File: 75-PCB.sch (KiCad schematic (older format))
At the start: 193 parts

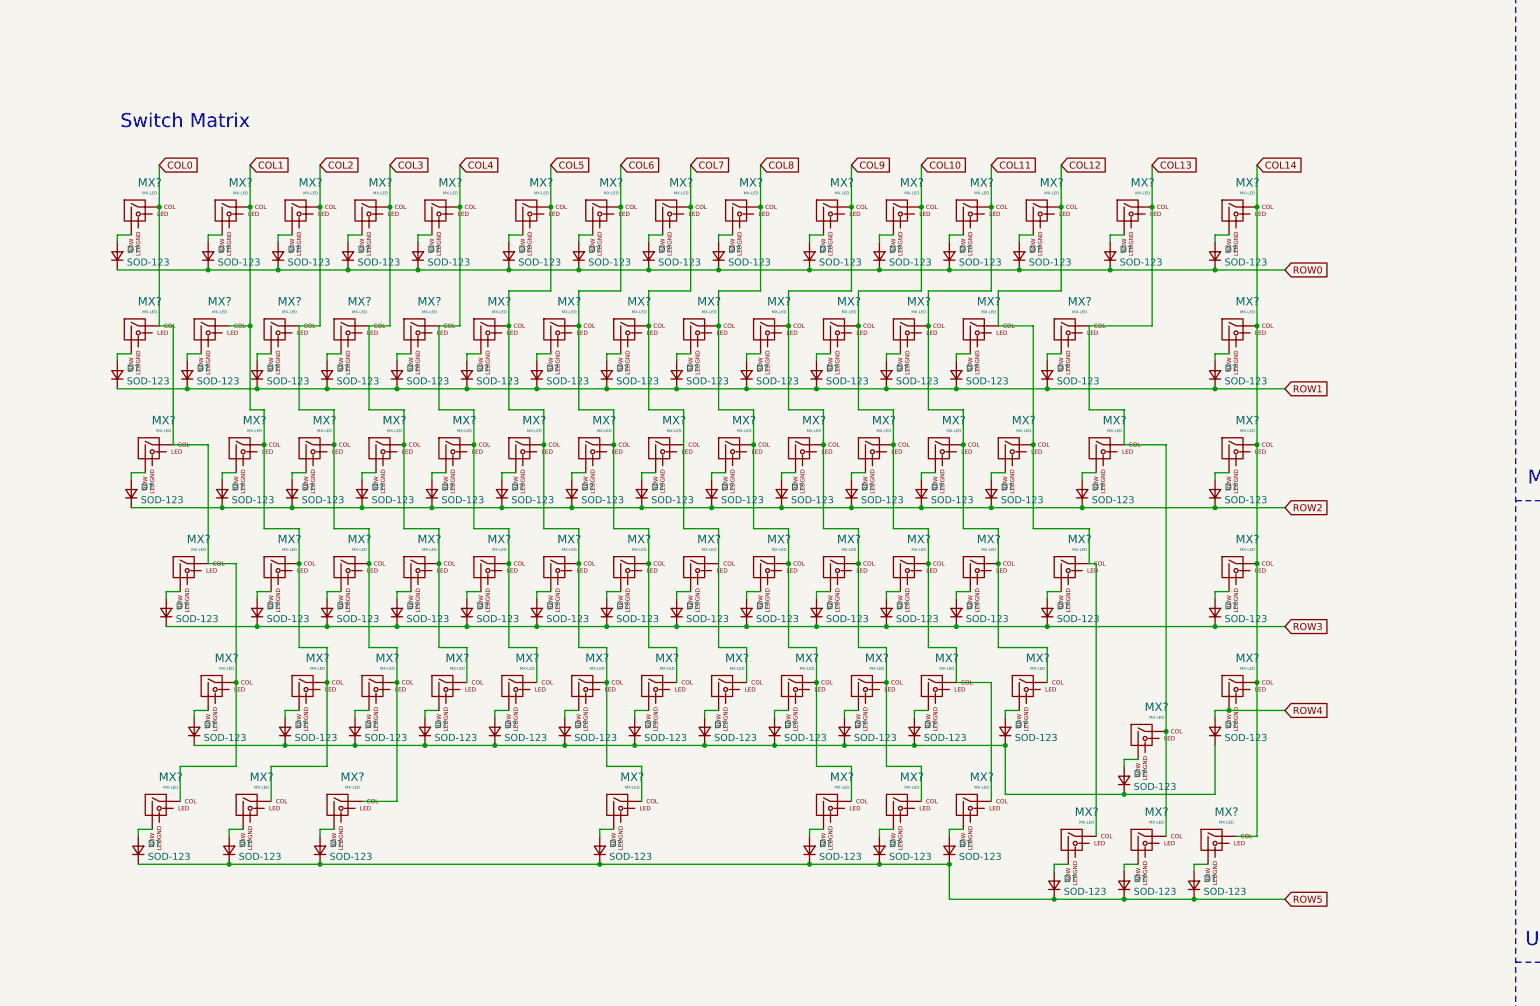
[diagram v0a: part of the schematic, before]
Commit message: Changed layout of switch matrix in schematic
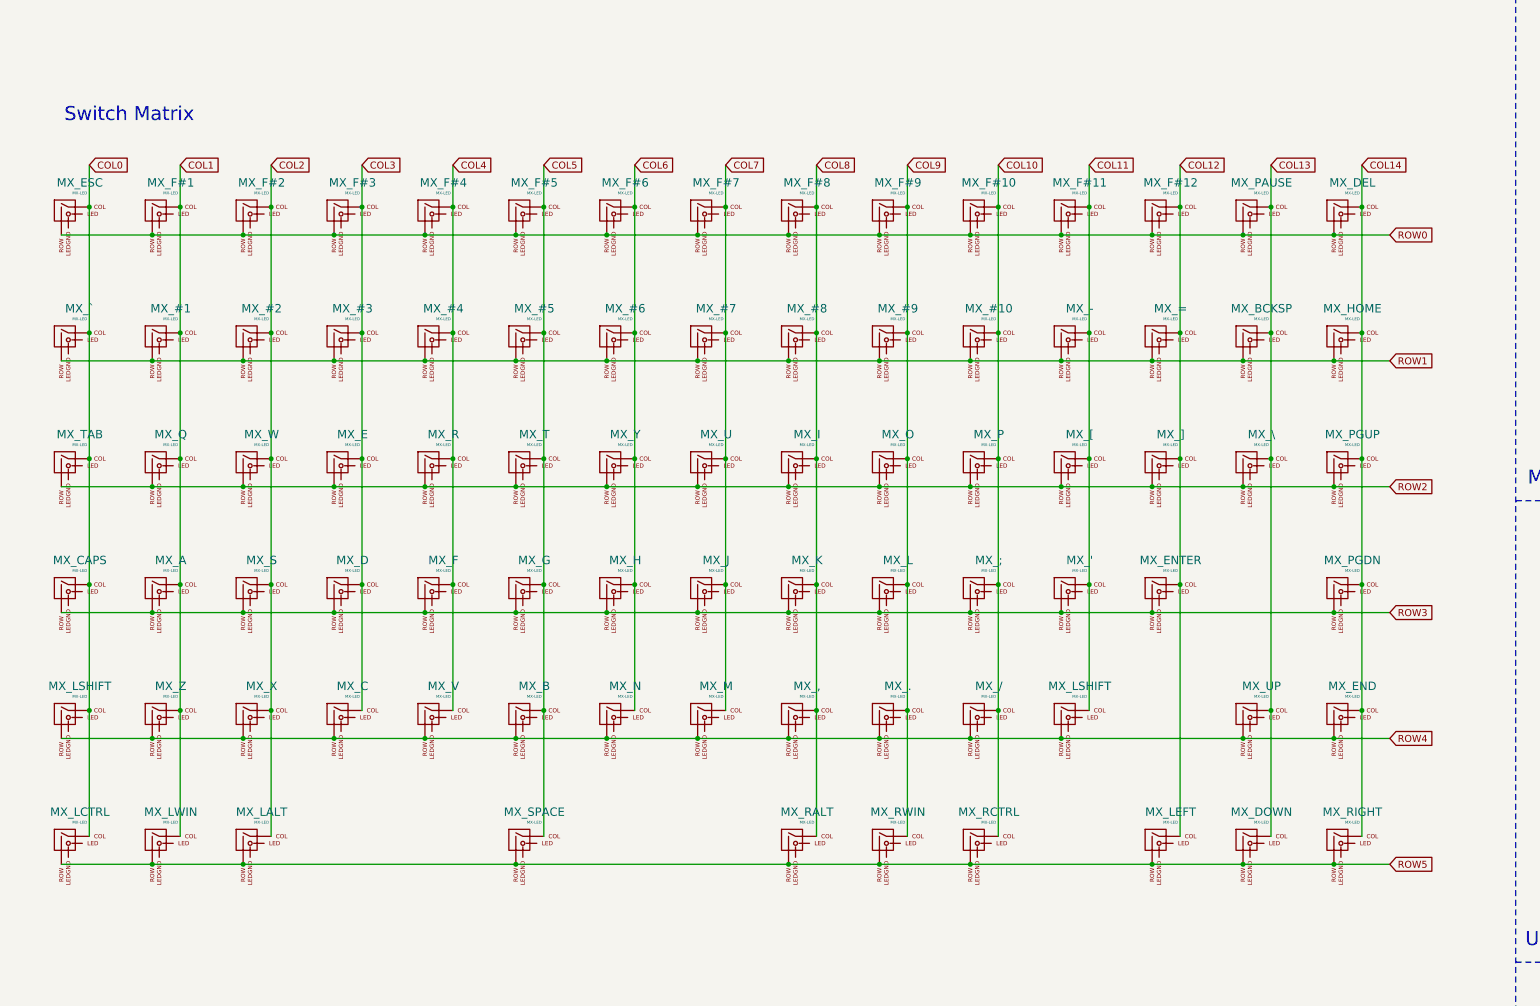
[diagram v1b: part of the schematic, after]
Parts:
- removed D? (x83): SOD-123, symbol Device:D_Small
- removed MX? (x83): MX-LED, symbol MX_Alps_Hybrid:MX-LED
- added MX_#1, MX_#10, MX_#2, MX_#3, MX_#4, MX_#5, MX_#6, MX_#7, MX_#8, MX_#9, MX_', MX_,, MX_-, MX_., MX_/, MX_;, MX_=, MX_A, MX_B, MX_BCKSP, MX_C, MX_CAPS, MX_D, MX_DEL, MX_DOWN, MX_E, MX_END, MX_ENTER, MX_ESC, MX_F, MX_F#1, MX_F#10, MX_F#11, MX_F#12, MX_F#2, MX_F#3, MX_F#4, MX_F#5, MX_F#6, MX_F#7, MX_F#8, MX_F#9, MX_G, MX_H, MX_HOME, MX_I, MX_J, MX_K, MX_L, MX_LALT, MX_LCTRL, MX_LEFT, MX_LSHIFT (x2), MX_LWIN, MX_M, MX_N, MX_O, MX_P, MX_PAUSE, MX_PGDN, MX_PGUP, MX_Q, MX_R, MX_RALT, MX_RCTRL, MX_RIGHT, MX_RWIN, MX_S, MX_SPACE, MX_T, MX_TAB, MX_U, MX_UP, MX_V, MX_W, MX_X, MX_Y, MX_Z, MX_[, MX_\, MX_], MX_`: MX-LED, symbol MX_Alps_Hybrid:MX-LED
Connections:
- net COL0: now also MX_CAPS.1 (COL), MX_ESC.1 (COL), MX_LCTRL.1 (COL), MX_LSHIFT.1 (COL), MX_TAB.1 (COL), MX_`.1 (COL)
- net COL1: now also MX_#1.1 (COL), MX_A.1 (COL), MX_F#1.1 (COL), MX_LWIN.1 (COL), MX_Q.1 (COL), MX_Z.1 (COL)
- net COL10: now also MX_#10.1 (COL), MX_/.1 (COL), MX_;.1 (COL), MX_F#10.1 (COL), MX_P.1 (COL), MX_RCTRL.1 (COL)
- net COL11: now also MX_'.1 (COL), MX_-.1 (COL), MX_F#11.1 (COL), MX_LSHIFT.1 (COL), MX_[.1 (COL)
- net COL12: now also MX_=.1 (COL), MX_ENTER.1 (COL), MX_F#12.1 (COL), MX_LEFT.1 (COL), MX_].1 (COL)
- net COL13: now also MX_BCKSP.1 (COL), MX_DOWN.1 (COL), MX_PAUSE.1 (COL), MX_UP.1 (COL), MX_\.1 (COL)
- net COL14: now also MX_DEL.1 (COL), MX_END.1 (COL), MX_HOME.1 (COL), MX_PGDN.1 (COL), MX_PGUP.1 (COL), MX_RIGHT.1 (COL)
- net COL2: now also MX_#2.1 (COL), MX_F#2.1 (COL), MX_LALT.1 (COL), MX_S.1 (COL), MX_W.1 (COL), MX_X.1 (COL)
- net COL3: now also MX_#3.1 (COL), MX_C.1 (COL), MX_D.1 (COL), MX_E.1 (COL), MX_F#3.1 (COL)
- net COL4: now also MX_#4.1 (COL), MX_F#4.1 (COL), MX_F.1 (COL), MX_R.1 (COL), MX_V.1 (COL)
- net COL5: now also MX_#5.1 (COL), MX_B.1 (COL), MX_F#5.1 (COL), MX_G.1 (COL), MX_SPACE.1 (COL), MX_T.1 (COL)
- net COL6: now also MX_#6.1 (COL), MX_F#6.1 (COL), MX_H.1 (COL), MX_N.1 (COL), MX_Y.1 (COL)
- net COL7: now also MX_#7.1 (COL), MX_F#7.1 (COL), MX_J.1 (COL), MX_M.1 (COL), MX_U.1 (COL)
- net COL8: now also MX_#8.1 (COL), MX_,.1 (COL), MX_F#8.1 (COL), MX_I.1 (COL), MX_K.1 (COL), MX_RALT.1 (COL)
- net COL9: now also MX_#9.1 (COL), MX_..1 (COL), MX_F#9.1 (COL), MX_L.1 (COL), MX_O.1 (COL), MX_RWIN.1 (COL)
- net ROW0: now also MX_DEL.2 (ROW), MX_ESC.2 (ROW), MX_F#1.2 (ROW), MX_F#10.2 (ROW), MX_F#11.2 (ROW), MX_F#12.2 (ROW), MX_F#2.2 (ROW), MX_F#3.2 (ROW), MX_F#4.2 (ROW), MX_F#5.2 (ROW), MX_F#6.2 (ROW), MX_F#7.2 (ROW), MX_F#8.2 (ROW), MX_F#9.2 (ROW), MX_PAUSE.2 (ROW)
- net ROW1: now also MX_#1.2 (ROW), MX_#10.2 (ROW), MX_#2.2 (ROW), MX_#3.2 (ROW), MX_#4.2 (ROW), MX_#5.2 (ROW), MX_#6.2 (ROW), MX_#7.2 (ROW), MX_#8.2 (ROW), MX_#9.2 (ROW), MX_-.2 (ROW), MX_=.2 (ROW), MX_BCKSP.2 (ROW), MX_HOME.2 (ROW), MX_`.2 (ROW)
- net ROW2: now also MX_E.2 (ROW), MX_I.2 (ROW), MX_O.2 (ROW), MX_P.2 (ROW), MX_PGUP.2 (ROW), MX_Q.2 (ROW), MX_R.2 (ROW), MX_T.2 (ROW), MX_TAB.2 (ROW), MX_U.2 (ROW), MX_W.2 (ROW), MX_Y.2 (ROW), MX_[.2 (ROW), MX_\.2 (ROW), MX_].2 (ROW)
- net ROW3: now also MX_'.2 (ROW), MX_;.2 (ROW), MX_A.2 (ROW), MX_CAPS.2 (ROW), MX_D.2 (ROW), MX_ENTER.2 (ROW), MX_F.2 (ROW), MX_G.2 (ROW), MX_H.2 (ROW), MX_J.2 (ROW), MX_K.2 (ROW), MX_L.2 (ROW), MX_PGDN.2 (ROW), MX_S.2 (ROW)
- net ROW4: now also MX_,.2 (ROW), MX_..2 (ROW), MX_/.2 (ROW), MX_B.2 (ROW), MX_C.2 (ROW), MX_END.2 (ROW), MX_LSHIFT.2 (ROW), MX_LSHIFT.2 (ROW), MX_M.2 (ROW), MX_N.2 (ROW), MX_UP.2 (ROW), MX_V.2 (ROW), MX_X.2 (ROW), MX_Z.2 (ROW)
- net ROW5: now also MX_DOWN.2 (ROW), MX_LALT.2 (ROW), MX_LCTRL.2 (ROW), MX_LEFT.2 (ROW), MX_LWIN.2 (ROW), MX_RALT.2 (ROW), MX_RCTRL.2 (ROW), MX_RIGHT.2 (ROW), MX_RWIN.2 (ROW), MX_SPACE.2 (ROW)

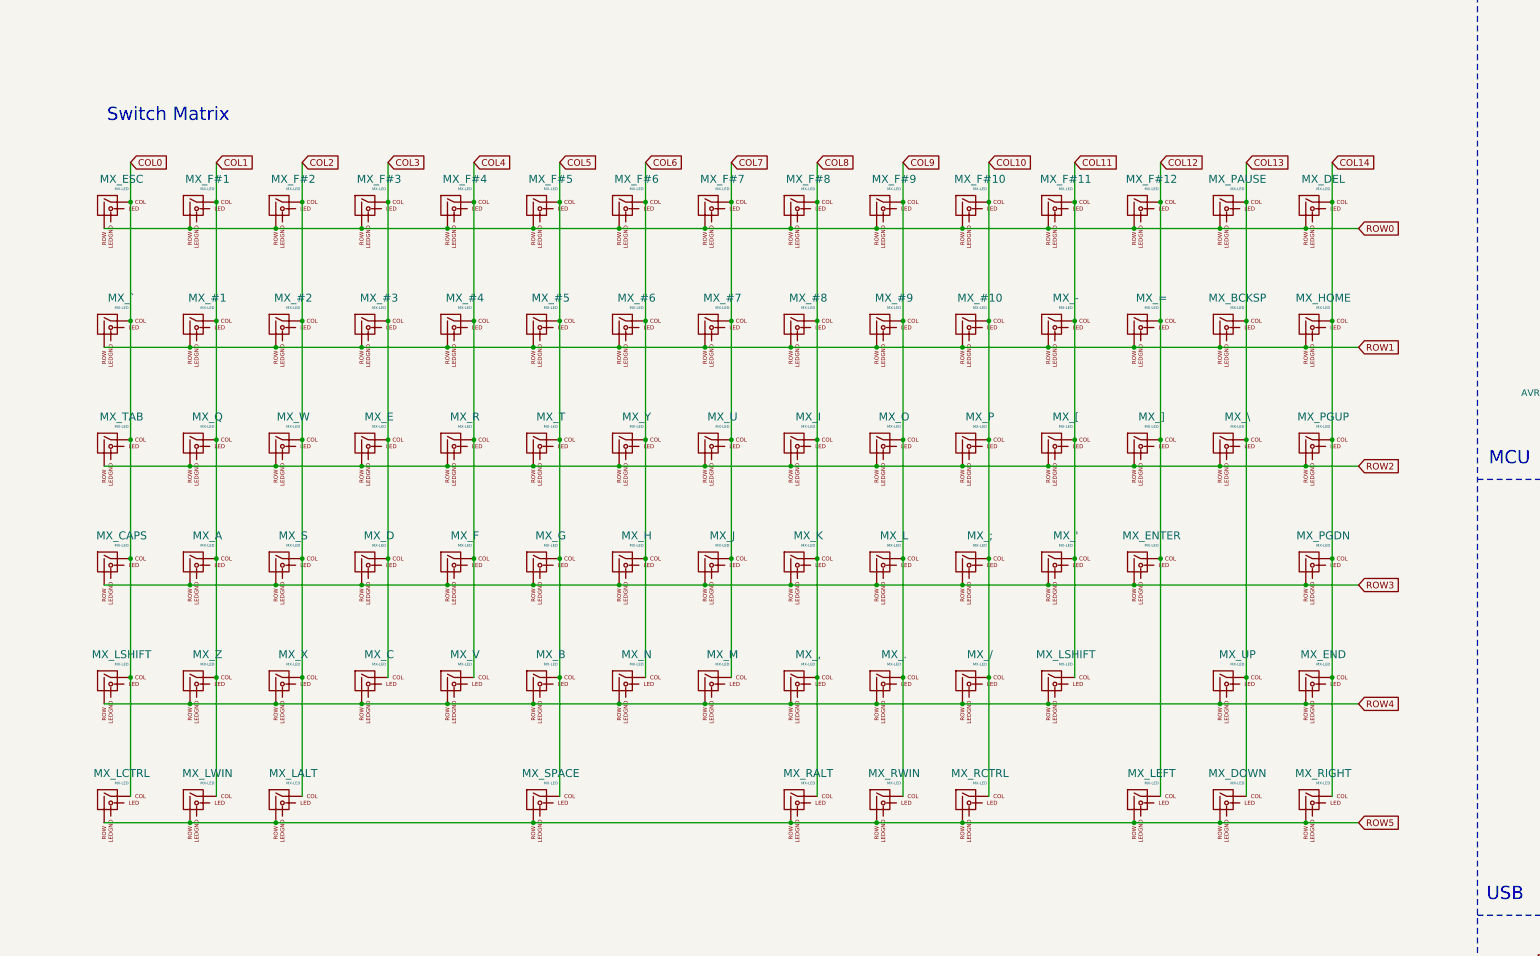
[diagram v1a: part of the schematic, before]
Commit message: Created copy of schematic for hot-swap implementation, added diodes and an extra switch symbol for split backspace support
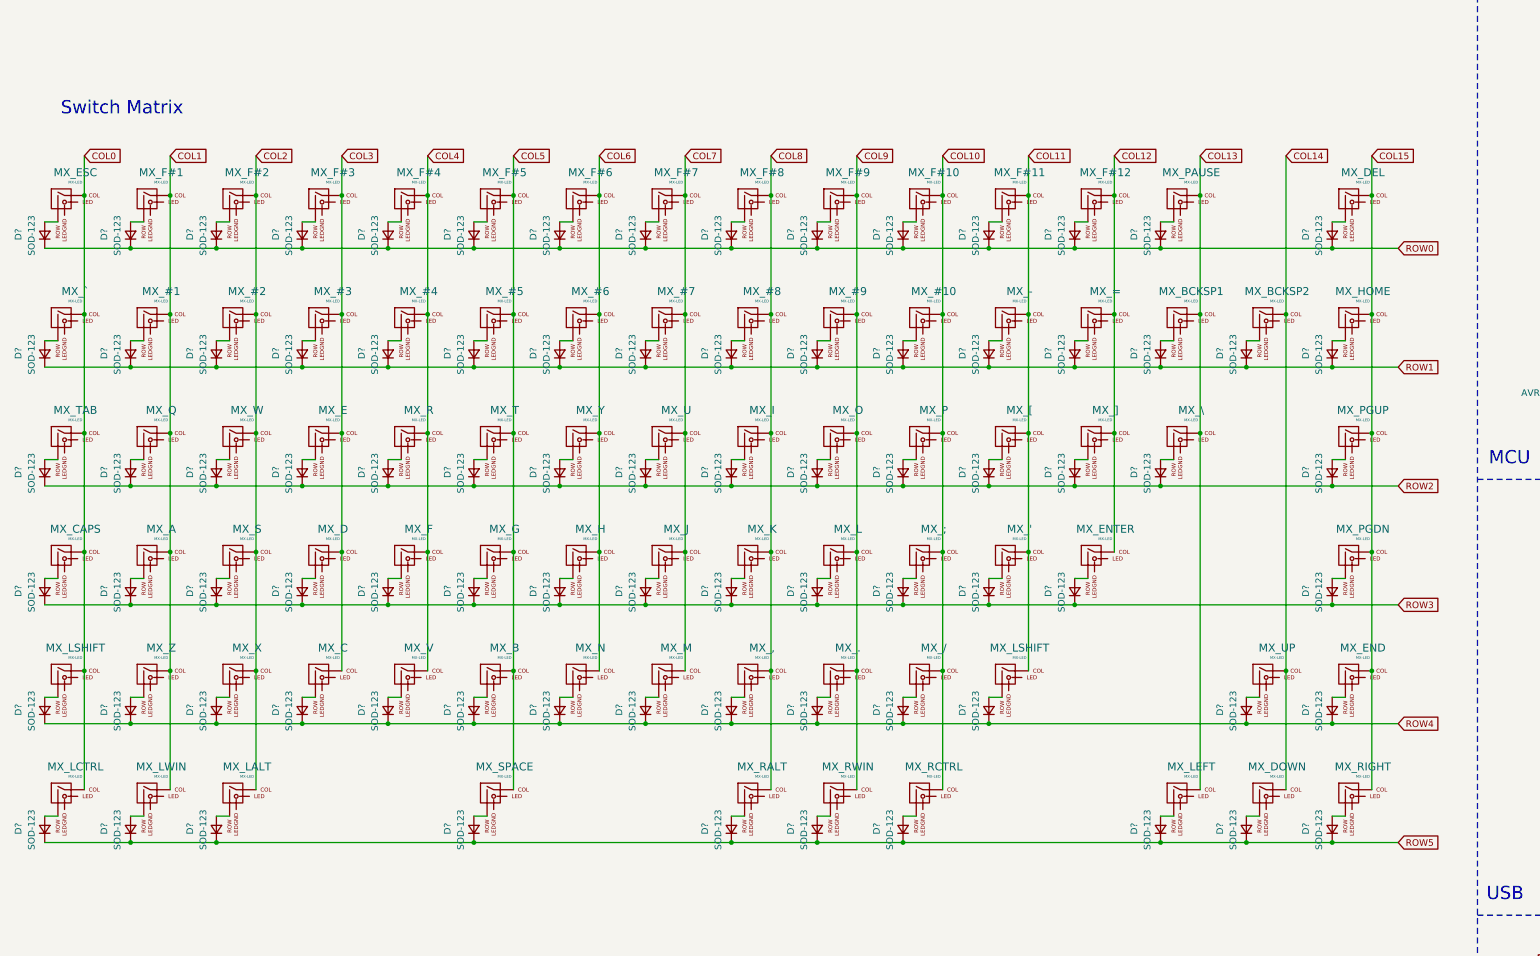
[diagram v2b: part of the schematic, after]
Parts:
- added D? (x84): SOD-123, symbol Device:D_Small
- added MX_BCKSP2: MX-LED, symbol MX_Alps_Hybrid:MX-LED
- renumbered MX_BCKSP to MX_BCKSP1
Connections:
- net COL12: no longer MX_LEFT.1 (COL)
- net COL13: now also MX_LEFT.1 (COL); no longer MX_DOWN.1 (COL), MX_UP.1 (COL)
- net COL14: now also MX_DOWN.1 (COL), MX_UP.1 (COL), MX_BCKSP2.1 (COL); no longer MX_DEL.1 (COL), MX_END.1 (COL), MX_HOME.1 (COL), MX_PGDN.1 (COL), MX_PGUP.1 (COL), MX_RIGHT.1 (COL)
- net ROW0: now also D?.1 (K), D?.1 (K), D?.1 (K), D?.1 (K), D?.1 (K), D?.1 (K), D?.1 (K), D?.1 (K), D?.1 (K), D?.1 (K), D?.1 (K), D?.1 (K), D?.1 (K), D?.1 (K), D?.1 (K); no longer MX_DEL.2 (ROW), MX_ESC.2 (ROW), MX_F#1.2 (ROW), MX_F#10.2 (ROW), MX_F#11.2 (ROW), MX_F#12.2 (ROW), MX_F#2.2 (ROW), MX_F#3.2 (ROW), MX_F#4.2 (ROW), MX_F#5.2 (ROW), MX_F#6.2 (ROW), MX_F#7.2 (ROW), MX_F#8.2 (ROW), MX_F#9.2 (ROW), MX_PAUSE.2 (ROW)
- net ROW1: now also D?.1 (K), D?.1 (K), D?.1 (K), D?.1 (K), D?.1 (K), D?.1 (K), D?.1 (K), D?.1 (K), D?.1 (K), D?.1 (K), D?.1 (K), D?.1 (K), D?.1 (K), D?.1 (K), D?.1 (K), D?.1 (K); no longer MX_#1.2 (ROW), MX_#10.2 (ROW), MX_#2.2 (ROW), MX_#3.2 (ROW), MX_#4.2 (ROW), MX_#5.2 (ROW), MX_#6.2 (ROW), MX_#7.2 (ROW), MX_#8.2 (ROW), MX_#9.2 (ROW), MX_-.2 (ROW), MX_=.2 (ROW), MX_BCKSP1.2 (ROW), MX_HOME.2 (ROW), MX_`.2 (ROW)
- net ROW2: now also D?.1 (K), D?.1 (K), D?.1 (K), D?.1 (K), D?.1 (K), D?.1 (K), D?.1 (K), D?.1 (K), D?.1 (K), D?.1 (K), D?.1 (K), D?.1 (K), D?.1 (K), D?.1 (K), D?.1 (K); no longer MX_E.2 (ROW), MX_I.2 (ROW), MX_O.2 (ROW), MX_P.2 (ROW), MX_PGUP.2 (ROW), MX_Q.2 (ROW), MX_R.2 (ROW), MX_T.2 (ROW), MX_TAB.2 (ROW), MX_U.2 (ROW), MX_W.2 (ROW), MX_Y.2 (ROW), MX_[.2 (ROW), MX_\.2 (ROW), MX_].2 (ROW)
- net ROW3: now also D?.1 (K), D?.1 (K), D?.1 (K), D?.1 (K), D?.1 (K), D?.1 (K), D?.1 (K), D?.1 (K), D?.1 (K), D?.1 (K), D?.1 (K), D?.1 (K), D?.1 (K), D?.1 (K); no longer MX_'.2 (ROW), MX_;.2 (ROW), MX_A.2 (ROW), MX_CAPS.2 (ROW), MX_D.2 (ROW), MX_ENTER.2 (ROW), MX_F.2 (ROW), MX_G.2 (ROW), MX_H.2 (ROW), MX_J.2 (ROW), MX_K.2 (ROW), MX_L.2 (ROW), MX_PGDN.2 (ROW), MX_S.2 (ROW)
- net ROW4: now also D?.1 (K), D?.1 (K), D?.1 (K), D?.1 (K), D?.1 (K), D?.1 (K), D?.1 (K), D?.1 (K), D?.1 (K), D?.1 (K), D?.1 (K), D?.1 (K), D?.1 (K), D?.1 (K); no longer MX_,.2 (ROW), MX_..2 (ROW), MX_/.2 (ROW), MX_B.2 (ROW), MX_C.2 (ROW), MX_END.2 (ROW), MX_LSHIFT.2 (ROW), MX_LSHIFT.2 (ROW), MX_M.2 (ROW), MX_N.2 (ROW), MX_UP.2 (ROW), MX_V.2 (ROW), MX_X.2 (ROW), MX_Z.2 (ROW)
- net ROW5: now also D?.1 (K), D?.1 (K), D?.1 (K), D?.1 (K), D?.1 (K), D?.1 (K), D?.1 (K), D?.1 (K), D?.1 (K), D?.1 (K); no longer MX_DOWN.2 (ROW), MX_LALT.2 (ROW), MX_LCTRL.2 (ROW), MX_LEFT.2 (ROW), MX_LWIN.2 (ROW), MX_RALT.2 (ROW), MX_RCTRL.2 (ROW), MX_RIGHT.2 (ROW), MX_RWIN.2 (ROW), MX_SPACE.2 (ROW)
- new net: D?.2 (A), MX_ESC.2 (ROW)
- new net: D?.2 (A), MX_F#1.2 (ROW)
- new net: D?.2 (A), MX_F#2.2 (ROW)
- new net: D?.2 (A), MX_F#3.2 (ROW)
- new net: D?.2 (A), MX_F#4.2 (ROW)
- new net: D?.2 (A), MX_F#5.2 (ROW)
- new net: D?.2 (A), MX_F#6.2 (ROW)
- new net: D?.2 (A), MX_F#7.2 (ROW)
- new net: D?.2 (A), MX_F#8.2 (ROW)
- new net: D?.2 (A), MX_F#9.2 (ROW)
- new net: D?.2 (A), MX_F#10.2 (ROW)
- new net: D?.2 (A), MX_F#11.2 (ROW)
- new net: D?.2 (A), MX_F#12.2 (ROW)
- new net: D?.2 (A), MX_PAUSE.2 (ROW)
- new net: D?.2 (A), MX_DEL.2 (ROW)
- new net: D?.2 (A), MX_HOME.2 (ROW)
- new net: D?.2 (A), MX_BCKSP1.2 (ROW)
- new net: D?.2 (A), MX_=.2 (ROW)
- new net: D?.2 (A), MX_-.2 (ROW)
- new net: D?.2 (A), MX_#10.2 (ROW)
- new net: D?.2 (A), MX_#9.2 (ROW)
- new net: D?.2 (A), MX_#8.2 (ROW)
- new net: D?.2 (A), MX_#7.2 (ROW)
- new net: D?.2 (A), MX_#6.2 (ROW)
- new net: D?.2 (A), MX_#5.2 (ROW)
- new net: D?.2 (A), MX_#4.2 (ROW)
- new net: D?.2 (A), MX_#3.2 (ROW)
- new net: D?.2 (A), MX_#2.2 (ROW)
- new net: D?.2 (A), MX_#1.2 (ROW)
- new net: D?.2 (A), MX_`.2 (ROW)
- new net: D?.2 (A), MX_TAB.2 (ROW)
- new net: D?.2 (A), MX_Q.2 (ROW)
- new net: D?.2 (A), MX_W.2 (ROW)
- new net: D?.2 (A), MX_E.2 (ROW)
- new net: D?.2 (A), MX_R.2 (ROW)
- new net: D?.2 (A), MX_T.2 (ROW)
- new net: D?.2 (A), MX_Y.2 (ROW)
- new net: D?.2 (A), MX_U.2 (ROW)
- new net: D?.2 (A), MX_I.2 (ROW)
- new net: D?.2 (A), MX_O.2 (ROW)
- new net: D?.2 (A), MX_P.2 (ROW)
- new net: D?.2 (A), MX_[.2 (ROW)
- new net: D?.2 (A), MX_].2 (ROW)
- new net: D?.2 (A), MX_\.2 (ROW)
- new net: D?.2 (A), MX_PGUP.2 (ROW)
- new net: D?.2 (A), MX_PGDN.2 (ROW)
- new net: D?.2 (A), MX_ENTER.2 (ROW)
- new net: D?.2 (A), MX_'.2 (ROW)
- new net: D?.2 (A), MX_;.2 (ROW)
- new net: D?.2 (A), MX_L.2 (ROW)
- new net: D?.2 (A), MX_K.2 (ROW)
- new net: D?.2 (A), MX_J.2 (ROW)
- new net: D?.2 (A), MX_H.2 (ROW)
- new net: D?.2 (A), MX_G.2 (ROW)
- new net: D?.2 (A), MX_F.2 (ROW)
- new net: D?.2 (A), MX_D.2 (ROW)
- new net: D?.2 (A), MX_S.2 (ROW)
- new net: D?.2 (A), MX_A.2 (ROW)
- new net: D?.2 (A), MX_CAPS.2 (ROW)
- new net: D?.2 (A), MX_LSHIFT.2 (ROW) (x2)
- new net: D?.2 (A), MX_Z.2 (ROW)
- new net: D?.2 (A), MX_X.2 (ROW)
- new net: D?.2 (A), MX_C.2 (ROW)
- new net: D?.2 (A), MX_V.2 (ROW)
- new net: D?.2 (A), MX_B.2 (ROW)
- new net: D?.2 (A), MX_N.2 (ROW)
- new net: D?.2 (A), MX_M.2 (ROW)
- new net: D?.2 (A), MX_,.2 (ROW)
- new net: D?.2 (A), MX_..2 (ROW)
- new net: D?.2 (A), MX_/.2 (ROW)
- new net: D?.2 (A), MX_UP.2 (ROW)
- new net: D?.2 (A), MX_END.2 (ROW)
- new net: D?.2 (A), MX_RIGHT.2 (ROW)
- new net: D?.2 (A), MX_DOWN.2 (ROW)
- new net: D?.2 (A), MX_LEFT.2 (ROW)
- new net: D?.2 (A), MX_RCTRL.2 (ROW)
- new net: D?.2 (A), MX_RWIN.2 (ROW)
- new net: D?.2 (A), MX_RALT.2 (ROW)
- new net: D?.2 (A), MX_SPACE.2 (ROW)
- new net: D?.2 (A), MX_LALT.2 (ROW)
- new net: D?.2 (A), MX_LWIN.2 (ROW)
- new net: D?.2 (A), MX_LCTRL.2 (ROW)
- new net: D?.2 (A), MX_BCKSP2.2 (ROW)
- new net COL15: MX_DEL.1 (COL), MX_END.1 (COL), MX_HOME.1 (COL), MX_PGDN.1 (COL), MX_PGUP.1 (COL), MX_RIGHT.1 (COL)
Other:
- moved on the sheet: MX_#1, MX_#10, MX_#2, MX_#3, MX_#4, MX_#5, MX_#6, MX_#7, MX_#8, MX_#9, MX_', MX_,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
